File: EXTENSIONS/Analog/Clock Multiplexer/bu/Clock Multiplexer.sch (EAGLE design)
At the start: 13 parts

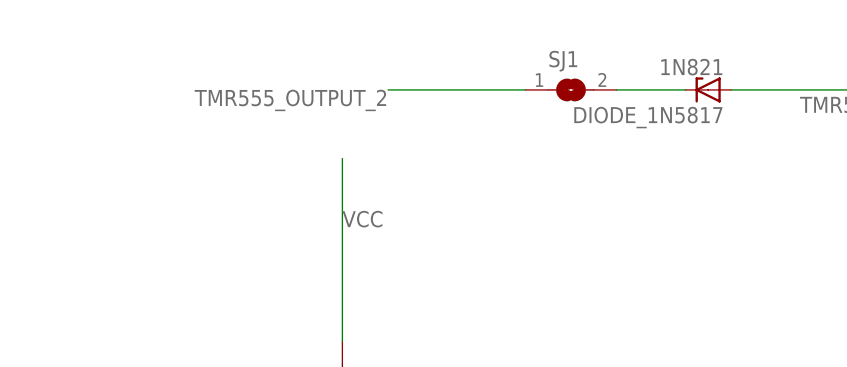
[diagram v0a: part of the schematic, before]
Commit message: update clock multiplexer
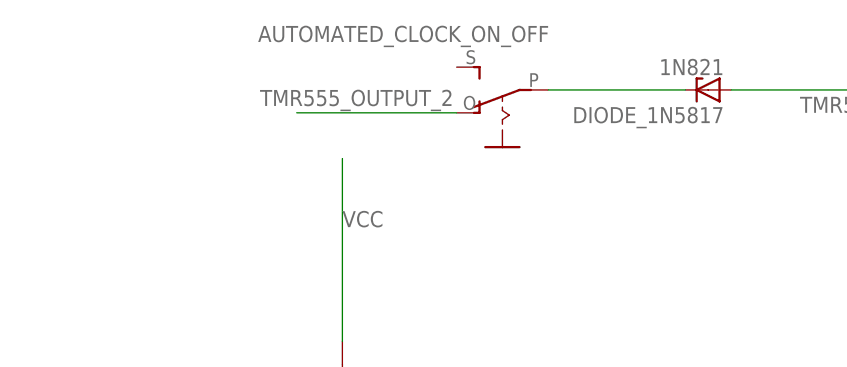
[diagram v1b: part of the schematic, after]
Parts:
- removed SJ1: (no value), microbuilder:SOLDERJUMPERREFLOW
- added AUTOMATED_CLOCK_ON_OFF: (no value), adafruit:EG1218S
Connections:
- net N$2: now also AUTOMATED_CLOCK_ON_OFF.P; no longer SJ1.2
- net TMR555_OUTPUT_2: now also AUTOMATED_CLOCK_ON_OFF.O; no longer SJ1.1
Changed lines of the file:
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@@
 <part name="R_MANUAL_CLOCK_PULL_DOWN" library="adafruit" deviceset="R-US_" device="R1206"/>
 <part name="GND9" library="supply1" deviceset="GND" device=""/>
-<part name="SJ1" library="microbuilder" deviceset="SOLDERJUMPER" device="REFLOW"/>
 <part name="DIODE_1N5817" library="diode" deviceset="1N821" device=""/>
+<part name="AUTOMATED_CLOCK_ON_OFF" library="adafruit" deviceset="EG1218" device="S"/>
 </parts>
 <sheets>
@@
 <instance part="R_MANUAL_CLOCK_PULL_DOWN" gate="G$1" x="-86.36" y="40.64"/>
 <instance part="GND9" gate="1" x="-106.68" y="40.64" rot="R270"/>
-<instance part="SJ1" gate="1" x="-40.64" y="129.54"/>
 <instance part="DIODE_1N5817" gate="1" x="-25.4" y="129.54" rot="R180"/>
+<instance part="AUTOMATED_CLOCK_ON_OFF" gate="1" x="-48.26" y="127" smashed="yes" rot="R90">
+<attribute name="NAME" x="-43.053" y="136.652" size="1.778" layer="95" rot="R180"/>
+<attribute name="VALUE" x="-51.435" y="123.19" size="1.778" layer="96" rot="R180"/>
+</instance>
 </instances>
 <busses>
@@
 </segment>
 <segment>
-<pinref part="SJ1" gate="1" pin="1"/>
-<wire x1="-45.72" y1="129.54" x2="-60.96" y2="129.54" width="0.1524" layer="91"/>
-<label x="-60.96" y="129.54" size="1.778" layer="95" rot="R180"/>
+<pinref part="AUTOMATED_CLOCK_ON_OFF" gate="1" pin="O"/>
+<wire x1="-53.34" y1="127" x2="-71.12" y2="127" width="0.1524" layer="91"/>
+<label x="-75.184" y="127.762" size="1.778" layer="95"/>
 </segment>
 </net>
@@
 <segment>
 <pinref part="DIODE_1N5817" gate="1" pin="C"/>
-<pinref part="SJ1" gate="1" pin="2"/>
-<wire x1="-27.94" y1="129.54" x2="-35.56" y2="129.54" width="0.1524" layer="91"/>
-</segment>
-</net>
+<pinref part="AUTOMATED_CLOCK_ON_OFF" gate="1" pin="P"/>
+<wire x1="-27.94" y1="129.54" x2="-43.18" y2="129.54" width="0.1524" layer="91"/>
+</segment>
+</net>

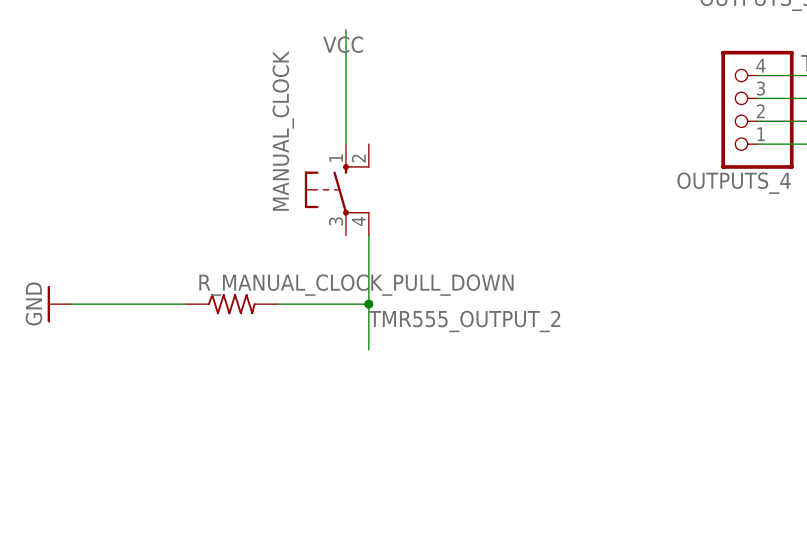
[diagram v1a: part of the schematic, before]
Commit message: update clock multiplexer
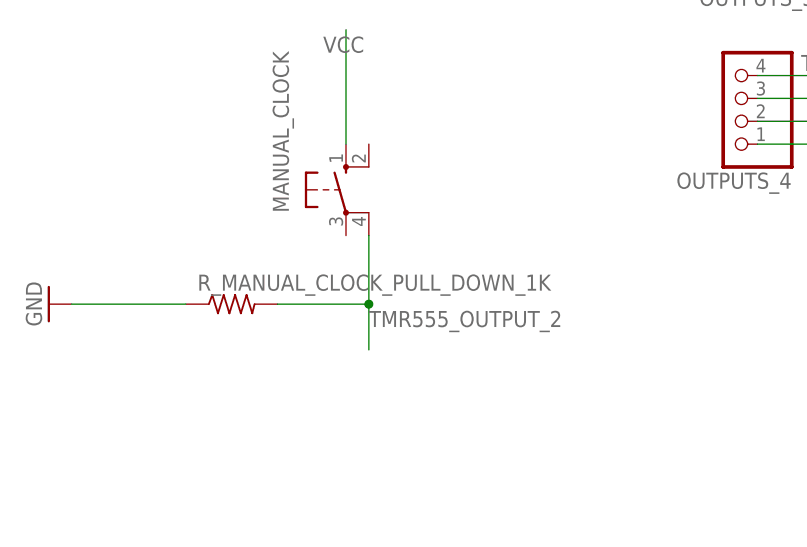
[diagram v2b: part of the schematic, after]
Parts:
- renumbered R_MANUAL_CLOCK_PULL_DOWN to R_MANUAL_CLOCK_PULL_DOWN_1K
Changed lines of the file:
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@@
 <part name="GND8" library="supply1" deviceset="GND" device=""/>
 <part name="MANUAL_CLOCK" library="switch-omron" deviceset="10-XX" device=""/>
-<part name="R_MANUAL_CLOCK_PULL_DOWN" library="adafruit" deviceset="R-US_" device="R1206"/>
+<part name="R_MANUAL_CLOCK_PULL_DOWN_1K" library="adafruit" deviceset="R-US_" device="R1206"/>
 <part name="GND9" library="supply1" deviceset="GND" device=""/>
 <part name="DIODE_1N5817" library="diode" deviceset="1N821" device=""/>
@@
 <instance part="GND8" gate="1" x="-66.04" y="81.28"/>
 <instance part="MANUAL_CLOCK" gate="1" x="-73.66" y="53.34"/>
-<instance part="R_MANUAL_CLOCK_PULL_DOWN" gate="G$1" x="-86.36" y="40.64"/>
+<instance part="R_MANUAL_CLOCK_PULL_DOWN_1K" gate="G$1" x="-86.36" y="40.64"/>
 <instance part="GND9" gate="1" x="-106.68" y="40.64" rot="R270"/>
 <instance part="DIODE_1N5817" gate="1" x="-25.4" y="129.54" rot="R180"/>
@@
 <segment>
 <pinref part="GND9" gate="1" pin="GND"/>
-<pinref part="R_MANUAL_CLOCK_PULL_DOWN" gate="G$1" pin="1"/>
+<pinref part="R_MANUAL_CLOCK_PULL_DOWN_1K" gate="G$1" pin="1"/>
 <wire x1="-104.14" y1="40.64" x2="-91.44" y2="40.64" width="0.1524" layer="91"/>
 </segment>
@@
 <wire x1="-71.12" y1="48.26" x2="-71.12" y2="40.64" width="0.1524" layer="91"/>
 <label x="-71.12" y="38.1" size="1.778" layer="95"/>
-<pinref part="R_MANUAL_CLOCK_PULL_DOWN" gate="G$1" pin="2"/>
+<pinref part="R_MANUAL_CLOCK_PULL_DOWN_1K" gate="G$1" pin="2"/>
 <wire x1="-71.12" y1="40.64" x2="-71.12" y2="35.56" width="0.1524" layer="91"/>
 <wire x1="-81.28" y1="40.64" x2="-71.12" y2="40.64" width="0.1524" layer="91"/>
